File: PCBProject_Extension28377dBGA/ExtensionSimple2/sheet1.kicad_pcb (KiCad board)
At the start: 4 copper layers, 88 parts, among them J1 Conn_02x05_Odd_Even, J2 Conn_01x02_Pin, J3 Conn_01x02_Pin, Q1 FMMT618TA, U1 SN74ABT541, U2 SN74ABT541

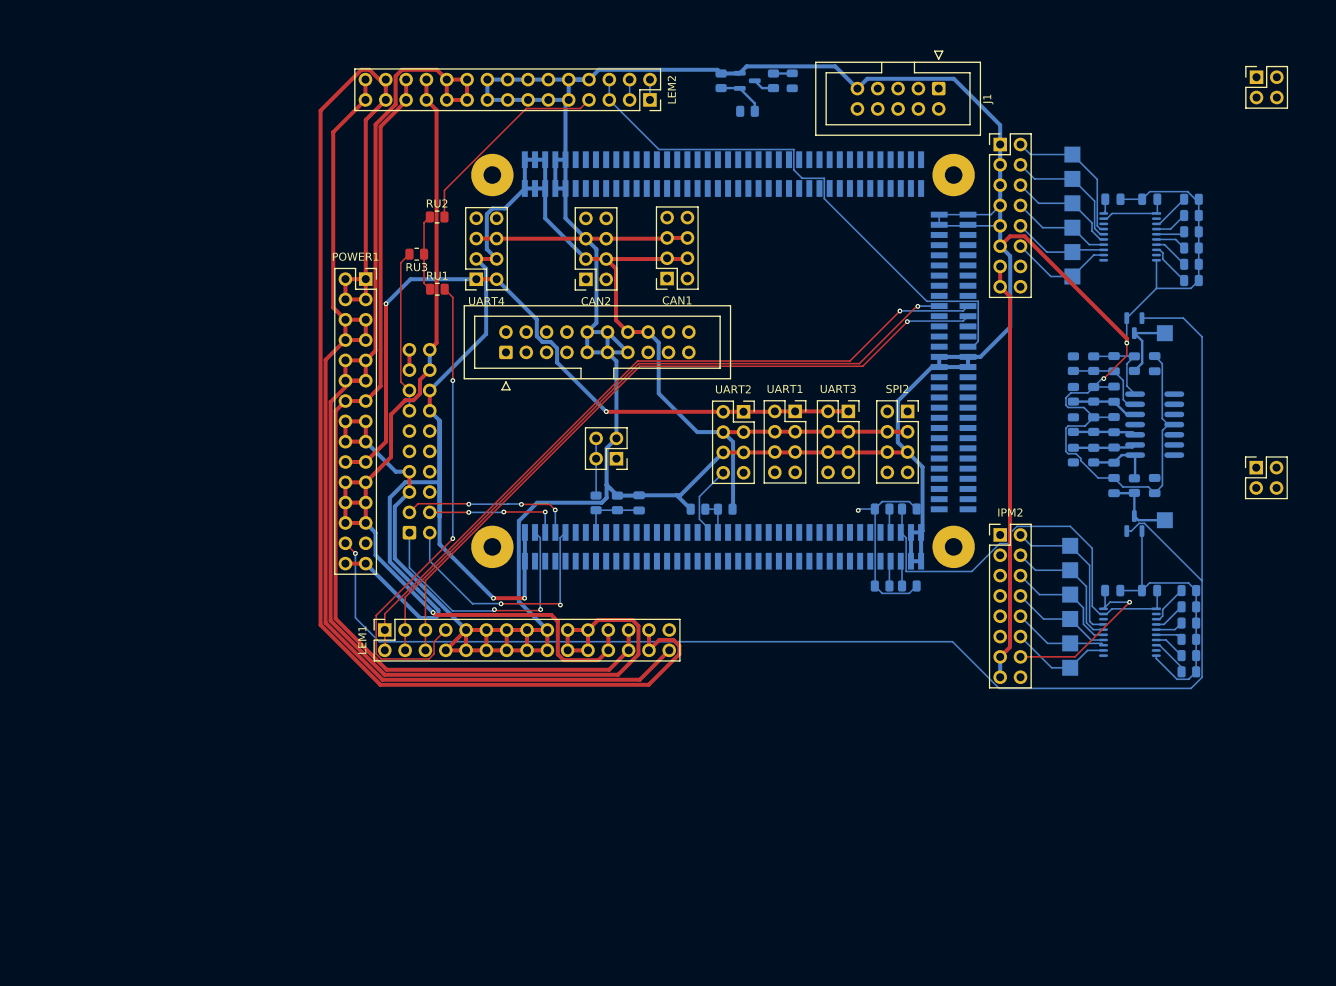
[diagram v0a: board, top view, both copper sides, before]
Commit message: HY finished layout GND铺铜
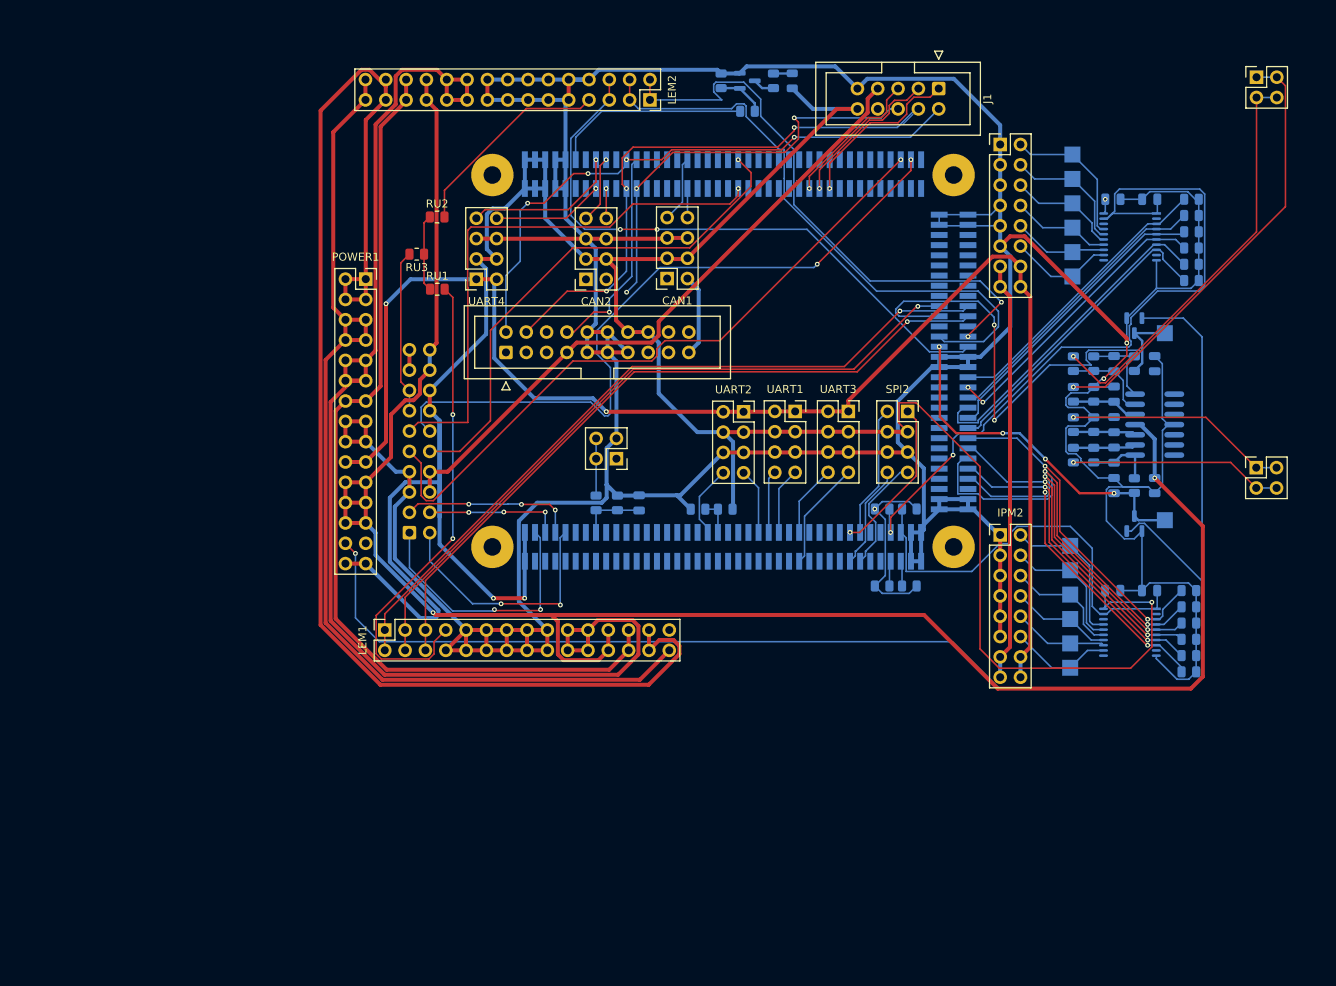
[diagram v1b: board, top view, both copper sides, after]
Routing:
- net VDD: track 0.00 -> 227.1 mm, vias 0 -> 3
- net D+5V: track 228.7 -> 382.1 mm, vias 2 -> 4
- net AGND: track 759.8 -> 633.7 mm, vias 3 -> 2
- net A+5V: track 139.9 -> 238.7 mm
- net /SPI_A_MI_HS: track 0.00 -> 88.1 mm, vias 0 -> 2
- net D12V1: track 92.2 -> 179.3 mm
- net /SPI_A_MO_HS: track 0.00 -> 84.5 mm, vias 0 -> 1
- net /DSP_PWM1~{_ENABL}E: track 11.7 -> 95.7 mm, vias 0 -> 2
- net PE_GND: track 0.00 -> 80.4 mm
- net /MQEP1A: track 0.00 -> 73.9 mm, vias 0 -> 4
- net /QEP1_HALL_U: track 0.00 -> 73.1 mm, vias 0 -> 1
- net /IPM_IV1: track 2.54 -> 74.8 mm
- net /IPM_IW1: track 2.54 -> 72.7 mm, vias 0 -> 2
- net /MQEP1B: track 0.00 -> 69.8 mm, vias 0 -> 3
- net /QEP1_HALL_W: track 0.00 -> 68.6 mm, vias 0 -> 1
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
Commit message: extension Update
need double check
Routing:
- net AGND: track 633.7 -> 267.7 mm, vias 2 -> 134
- net VDD: track 227.1 -> 165.7 mm, vias 3 -> 1
- net +12: track 170.1 -> 118.2 mm
- net Net-(LEM1-Pad7): track 0.00 -> 44.7 mm, vias 0 -> 2
- net /IPM_IV1: track 74.8 -> 118.3 mm
- net D+5V: track 382.1 -> 354.1 mm, vias 4 -> 5
- net /DSP-PWM6B: track 30.5 -> 51.9 mm
- net /DSP-PWM5A: track 50.7 -> 40.1 mm
- net 12VGND: track 160.6 -> 153.0 mm
- net AVDD: track 183.7 -> 177.8 mm, vias 1 -> 0
- net /IPM_IV2: track 88.5 -> 92.8 mm
- net /IPM_IW1: track 72.7 -> 76.4 mm
- net /IPM_IU2: track 90.2 -> 93.9 mm
- net /DSP-PWM6A: track 42.8 -> 39.4 mm
- net /DSP-PWM4B: track 40.4 -> 43.6 mm
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- added copper zone on In1.Cu, net AGND
- added copper zone on In2.Cu, net AGND

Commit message: submit extension board
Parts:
- moved C10 5.21 mm to (291.8, 128.9)
- moved C7 5.21 mm to (291.8, 125.1)
- moved IPM2 5.21 mm to (280.1, 135.0)
- moved J2 5.21 mm to (309.6, 126.6)
- moved U2 5.21 mm to (297.8, 143.8)
- moved C6 5.21 mm to (291.8, 117.4)
- moved C8 5.21 mm to (291.8, 113.6)
- moved U1 5.21 mm to (297.8, 94.4)
- moved C12 5.21 mm to (232.5, 131.0)
- moved R24 5.21 mm to (229.8, 131.0)
- moved C5 5.21 mm to (291.8, 121.3)
- moved J3 5.21 mm to (309.6, 77.8)
- moved CAN1 5.21 mm to (236.0, 103.0)
- moved DI1 5.21 mm to (229.6, 125.5)
- moved INC1 5.21 mm to (215.8, 112.2)
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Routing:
- net VDD: track 165.7 -> 216.5 mm, vias 1 -> 4
- net AGND: track 267.7 -> 259.8 mm, vias 134 -> 145
- net /QEP1_HALL_U: track 73.1 -> 69.6 mm
- net /IPM_IW1: track 76.4 -> 74.4 mm
- net /MQEP1S: track 26.8 -> 26.0 mm
- net /~{SPI_A_STE_HS}: track 64.5 -> 65.3 mm
- net /QEP1_HALL_V: track 65.1 -> 64.4 mm
- net D+5V: vias 5 -> 2
- net (no net): vias 15 -> 0
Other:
- board outline added: 122.2 x 82.1 mm
- board text added: "_(:з」∠)_ 2024-01-06 Project Eureka Redesign"

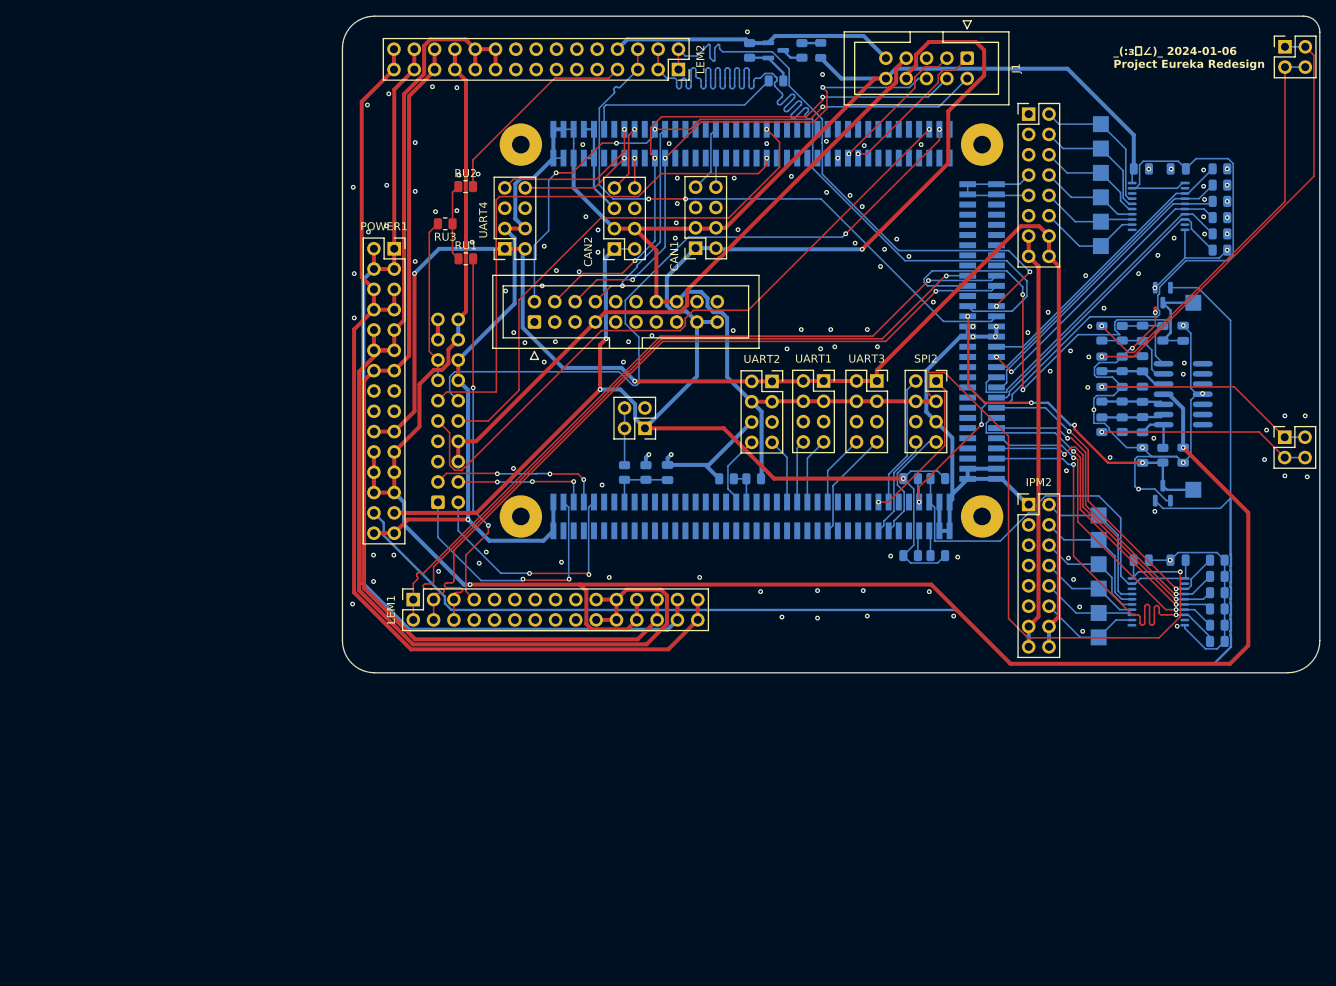
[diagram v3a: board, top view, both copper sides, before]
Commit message: add some text items
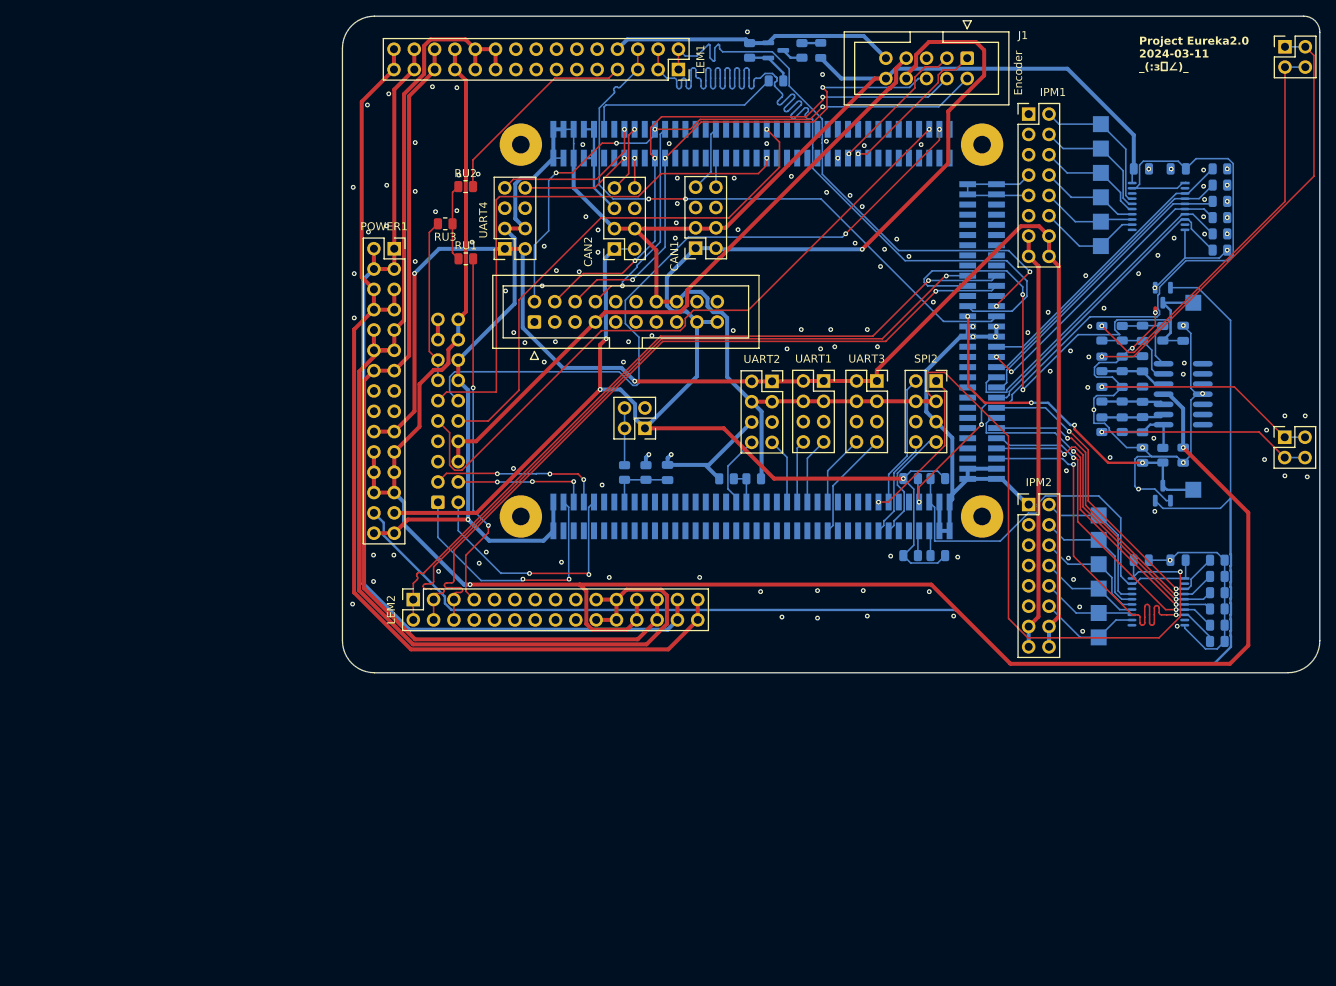
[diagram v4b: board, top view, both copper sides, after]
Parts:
- R21, R22: value 1k -> 1K
- R31: value 301R -> 1K
- renumbered LEM2 to LEM1, LEM1 to LEM2
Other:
- board text added: "Encoder"
- board text added: "IPM1"
- board text added: "Project Eureka2.0 2024-03-11 _(:з」∠)_"
- board text removed: "_(:з」∠)_ 2024-01-06 Project Eureka Redesign"
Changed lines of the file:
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@@
       (net 212 "REF_3V") (pinfunction "1") (pintype "passive"))
     (pad "2" smd roundrect (at 0.9125 0) (size 1.025 1.4) (layers "F.Cu" "F.Paste" "F.Mask") (roundrect_rratio 0.243902439)
-      (net 213 "Net-(LEM2-Pad7)") (pinfunction "2") (pintype "passive"))
+      (net 72 "Net-(LEM1-Pad7)") (pinfunction "2") (pintype "passive"))
     (model "${KICAD6_3DMODEL_DIR}/Resistor_SMD.3dshapes/R_0805_2012Metric.wrl"
       (offset (xyz 0 0 0))
@@
     (property "ki_keywords" "connector")
     (attr through_hole)
-    (fp_text reference "J1" (at 1.27 -6.1 90) (layer "F.SilkS")
+    (fp_text reference "J1" (at -2.8498 -6.9788 -180) (layer "F.SilkS")
         (effects (font (size 1 1) (thickness 0.15)))
     )
@@
       (net 212 "REF_3V") (pinfunction "1") (pintype "passive"))
     (pad "2" smd roundrect (at 0.9125 0) (size 1.025 1.4) (layers "F.Cu" "F.Paste" "F.Mask") (roundrect_rratio 0.243902439)
-      (net 72 "Net-(LEM1-Pad7)") (pinfunction "2") (pintype "passive"))
+      (net 213 "Net-(LEM2-Pad7)") (pinfunction "2") (pintype "passive"))
     (model "${KICAD6_3DMODEL_DIR}/Resistor_SMD.3dshapes/R_0805_2012Metric.wrl"
       (offset (xyz 0 0 0))
@@
     (property "ki_description" "Connector")
     (attr through_hole)
-    (fp_text reference "LEM2" (at -1.27 -2.77 90) (layer "F.SilkS")
+    (fp_text reference "LEM1" (at -1.27 -2.77 90) (layer "F.SilkS")
         (effects (font (size 1 1) (thickness 0.15)))
     )
@@
       (net 32 "/IPM_IU1") (pinfunction "6") (pintype "passive"))
     (pad "7" thru_hole oval (at 0 7.62 270) (size 1.7 1.7) (drill 1) (layers "*.Cu" "*.Mask")
-      (net 213 "Net-(LEM2-Pad7)") (pinfunction "7") (pintype "passive"))
+      (net 72 "Net-(LEM1-Pad7)") (pinfunction "7") (pintype "passive"))
     (pad "8" thru_hole oval (at -2.54 7.62 270) (size 1.7 1.7) (drill 1) (layers "*.Cu" "*.Mask")
       (net 1 "AGND") (pinfunction "8") (pintype "passive"))
@@
     (property "ki_keywords" "connector")
     (attr through_hole)
-    (fp_text reference "IPM1" (at -1.27 18.01) (layer "F.SilkS") hide
+    (fp_text reference "IPM1" (at -1.295285 6.8788 90) (layer "F.SilkS") hide
         (effects (font (size 1 1) (thickness 0.15)))
     )
@@
     (property "ki_description" "Connector")
     (attr through_hole)
-    (fp_text reference "LEM1" (at -1.27 -2.77 90) (layer "F.SilkS")
+    (fp_text reference "LEM2" (at -1.27 -2.77 90) (layer "F.SilkS")
         (effects (font (size 1 1) (thickness 0.15)))
     )
@@
       (net 35 "/IPM_IU2") (pinfunction "6") (pintype "passive"))
     (pad "7" thru_hole oval (at 0 7.62 90) (size 1.7 1.7) (drill 1) (layers "*.Cu" "*.Mask")
-      (net 72 "Net-(LEM1-Pad7)") (pinfunction "7") (pintype "passive"))
+      (net 213 "Net-(LEM2-Pad7)") (pinfunction "7") (pintype "passive"))
     (pad "8" thru_hole oval (at -2.54 7.62 90) (size 1.7 1.7) (drill 1) (layers "*.Cu" "*.Mask")
       (net 1 "AGND") (pinfunction "8") (pintype "passive"))
@@
         (effects (font (size 1 1) (thickness 0.15)) (justify mirror))
     )
-    (fp_text value "1k" (at 0 -1.65 90) (layer "B.Fab") hide
+    (fp_text value "1K" (at 0 -1.65 90) (layer "B.Fab") hide
         (effects (font (size 1 1) (thickness 0.15)) (justify mirror))
     )
@@
         (effects (font (size 1 1) (thickness 0.15)) (justify mirror))
     )
-    (fp_text value "1k" (at 0 -1.65 90) (layer "B.Fab") hide
+    (fp_text value "1K" (at 0 -1.65 90) (layer "B.Fab") hide
         (effects (font (size 1 1) (thickness 0.15)) (justify mirror))
     )
@@
         (effects (font (size 1 1) (thickness 0.15)) (justify mirror))
     )
-    (fp_text value "301R" (at 0 -1.65 90) (layer "B.Fab") hide
+    (fp_text value "1K" (at 0 -1.65 90) (layer "B.Fab") hide
         (effects (font (size 1 1) (thickness 0.15)) (justify mirror))
     )
@@
   (gr_line (start 195.826 156.0674) (end 310 156.0674)
     (stroke (width 0.05) (type default)) (layer "Edge.Cuts"))
-  (gr_text "_(:з」∠)_ 2024-01-06 \nProject Eureka Redesign" (at 288.1936 80.5786) (layer "F.SilkS")
+  (gr_text "Encoder" (at 276.9 83.9 90) (layer "F.SilkS")
+    (effects (font (size 1 1) (thickness 0.1)) (justify left bottom))
+  )
+  (gr_text "IPM1" (at 279 84.1) (layer "F.SilkS")
+    (effects (font (size 1 1) (thickness 0.1)) (justify left bottom))
+  )
+  (gr_text "Project Eureka2.0\n2024-03-11 \n_(:з」∠)_ " (at 291.4 80.9) (layer "F.SilkS")
     (effects (font (size 1 1) (thickness 0.2) bold) (justify left bottom))
   )
@@
   (segment (start 226.8272 107.1978) (end 226.8272 107.7058) (width 0.2) (layer "B.Cu") (net 49))
   (segment (start 231.556 102.231709) (end 228.640909 105.1468) (width 0.2) (layer "B.Cu") (net 49))
-  (segment (start 208.1612 120.448746) (end 208.168754 120.4563) (width 0.2) (layer "F.Cu") (net 72))
-  (segment (start 208.1612 104.3248) (end 208.1612 120.448746) (width 0.2) (layer "F.Cu") (net 72))
-  (segment (start 207.2502 141.3798) (end 210.068412 138.561588) (width 0.2) (layer "F.Cu") (net 72))
-  (segment (start 207.2502 145.8738) (end 207.2502 141.3798) (width 0.2) (layer "F.Cu") (net 72))
-  (segment (start 208.069976 146.693576) (end 207.2502 145.8738) (width 0.2) (layer "F.Cu") (net 72))
-  (segment (start 210.068412 138.561588) (end 210.068412 137.6544) (width 0.2) (layer "F.Cu") (net 72))
-  (via (at 208.168754 120.4563) (size 0.6) (drill 0.3) (layers "F.Cu" "B.Cu") (net 72))
-  (via (at 210.068412 137.6544) (size 0.6) (drill 0.3) (layers "F.Cu" "B.Cu") (net 72))
-  (segment (start 208.168754 120.4563) (end 208.168754 135.754742) (width 0.2) (layer "B.Cu") (net 72))
-  (segment (start 208.168754 135.754742) (end 210.068412 137.6544) (width 0.2) (layer "B.Cu") (net 72))
+  (segment (start 208.1362 95.2998) (end 208.1362 91.975107) (width 0.2) (layer "F.Cu") (net 72))
+  (segment (start 225.1292 81.7418) (end 226.2062 80.6648) (width 0.2) (layer "F.Cu") (net 72))
+  (segment (start 218.369507 81.7418) (end 225.1292 81.7418) (width 0.2) (layer "F.Cu") (net 72))
+  (segment (start 208.1362 91.975107) (end 218.369507 81.7418) (width 0.2) (layer "F.Cu") (net 72))
   (segment (start 202.0362 77.699559) (end 202.837959 76.8978) (width 0.5) (layer "F.Cu") (net 73))
   (segment (start 232.3882 146.416559) (end 231.646441 145.6748) (width 0.5) (layer "F.Cu") (net 73))
@@
   (segment (start 205.5862 103.5748) (end 206.3362 104.3248) (width 0.2) (layer "F.Cu") (net 212))
   (segment (start 205.5862 99.9498) (end 205.5862 96.0248) (width 0.2) (layer "F.Cu") (net 212))
-  (segment (start 208.1362 95.2998) (end 208.1362 91.975107) (width 0.2) (layer "F.Cu") (net 213))
-  (segment (start 225.1292 81.7418) (end 226.2062 80.6648) (width 0.2) (layer "F.Cu") (net 213))
-  (segment (start 218.369507 81.7418) (end 225.1292 81.7418) (width 0.2) (layer "F.Cu") (net 213))
-  (segment (start 208.1362 91.975107) (end 218.369507 81.7418) (width 0.2) (layer "F.Cu") (net 213))
+  (segment (start 208.1612 120.448746) (end 208.168754 120.4563) (width 0.2) (layer "F.Cu") (net 213))
+  (segment (start 208.1612 104.3248) (end 208.1612 120.448746) (width 0.2) (layer "F.Cu") (net 213))
+  (segment (start 207.2502 141.3798) (end 210.068412 138.561588) (width 0.2) (layer "F.Cu") (net 213))
+  (segment (start 207.2502 145.8738) (end 207.2502 141.3798) (width 0.2) (layer "F.Cu") (net 213))
+  (segment (start 208.069976 146.693576) (end 207.2502 145.8738) (width 0.2) (layer "F.Cu") (net 213))
+  (segment (start 210.068412 138.561588) (end 210.068412 137.6544) (width 0.2) (layer "F.Cu") (net 213))
+  (via (at 208.168754 120.4563) (size 0.6) (drill 0.3) (layers "F.Cu" "B.Cu") (net 213))
+  (via (at 210.068412 137.6544) (size 0.6) (drill 0.3) (layers "F.Cu" "B.Cu") (net 213))
+  (segment (start 208.168754 120.4563) (end 208.168754 135.754742) (width 0.2) (layer "B.Cu") (net 213))
+  (segment (start 208.168754 135.754742) (end 210.068412 137.6544) (width 0.2) (layer "B.Cu") (net 213))
   (segment (start 246.9322 81.101632) (end 245.055368 79.2248) (width 0.3) (layer "B.Cu") (net 227))
   (segment (start 246.9322 82.0848) (end 246.9322 81.101632) (width 0.3) (layer "B.Cu") (net 227))
